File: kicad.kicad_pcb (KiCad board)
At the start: 2 copper layers, 68.6 x 53.3 mm, 8 parts, among them P1 Power, P2 Analog, P3 Digital, P4 Digital, P5 CONN_01X01, P6 CONN_01X01, P7 CONN_01X01, P8 CONN_01X01

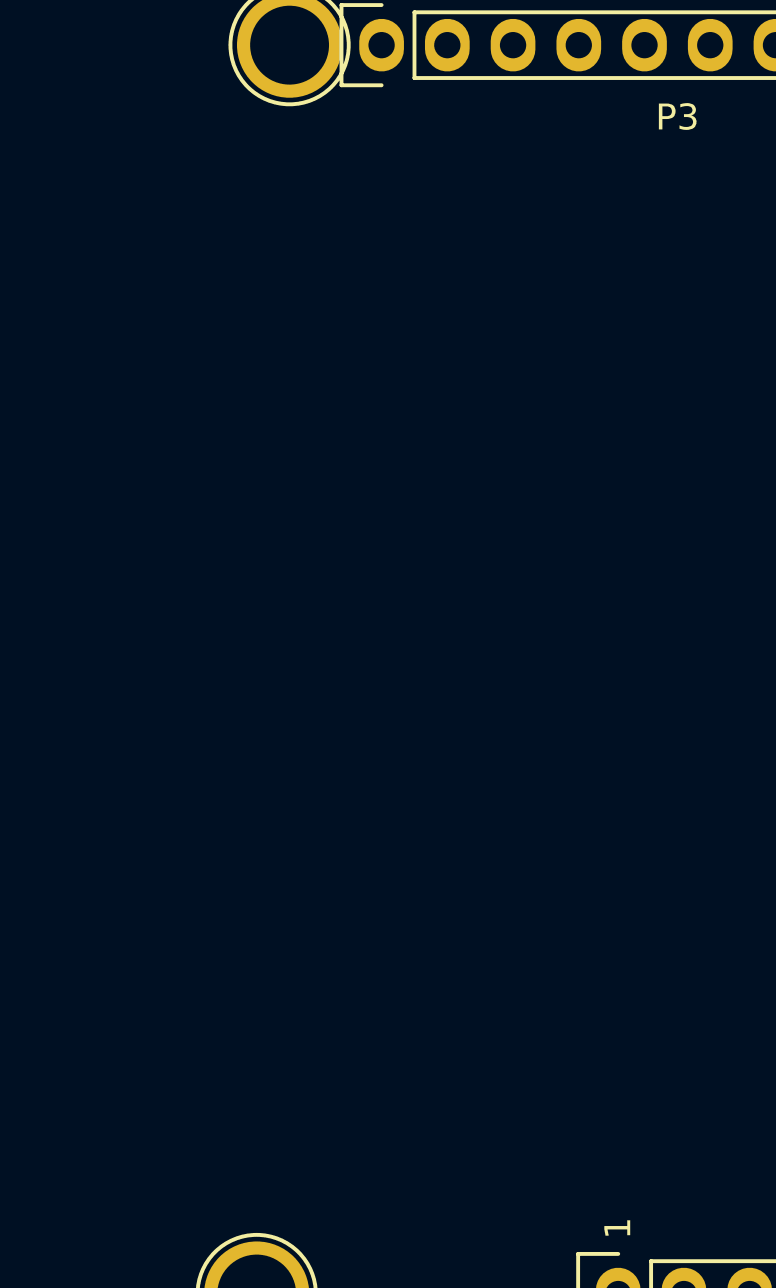
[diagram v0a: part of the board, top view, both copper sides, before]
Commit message: Add ATmega328P-PU
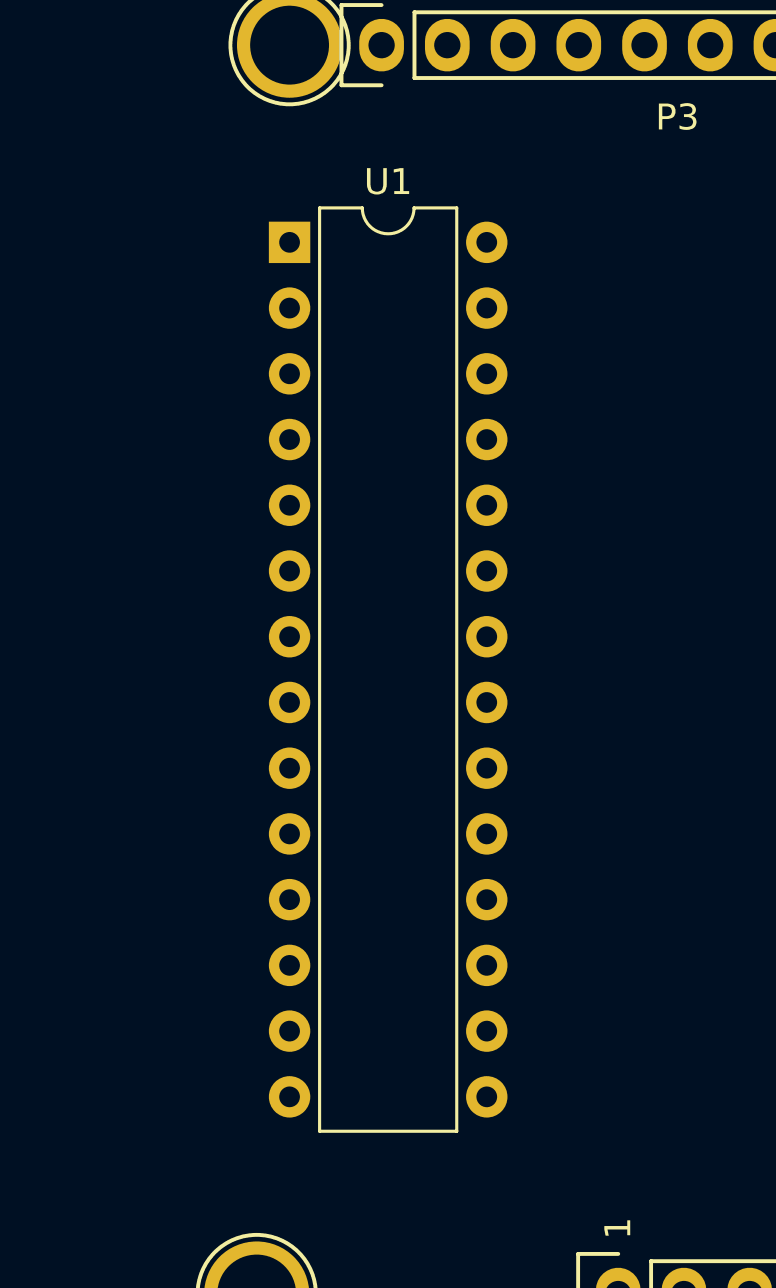
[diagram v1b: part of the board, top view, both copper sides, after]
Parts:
- added U1: ATmega328P-PU, Package_DIP:DIP-28_W7.62mm, F.Cu at (126.2, 83.2)
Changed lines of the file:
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@@
-(kicad_pcb (version 4) (host pcbnew 4.0.2-4+6225~38~ubuntu14.04.1-stable)
+(kicad_pcb (version 20171130) (host pcbnew 5.0.0+dfsg1-2)
   (general
-    (links 4)
-    (no_connects 4)
-    (area 104.572999 71.392 182.146334 127.594)
     (thickness 1.6)
     (drawings 27)
     (tracks 0)
     (zones 0)
-    (modules 8)
-    (nets 33)
+    (modules 9)
+    (nets 60)
   )
   (page A4)
@@
       (layerselection 0x00030_80000001)
       (usegerberextensions false)
+      (usegerberattributes false)
+      (usegerberadvancedattributes false)
+      (creategerberjobfile false)
       (excludeedgelayer true)
       (linewidth 0.100000)
@@
       (hpglpennumber 1)
       (hpglpenspeed 20)
-      (hpglpendiameter 15)
-      (hpglpenoverlay 2)
+      (hpglpendiameter 15.000000)
       (psnegative false)
       (psa4output false)
@@
   (net 31 "/12(MISO)")
   (net 32 "/11(**/MOSI)")
+  (net 33 "Net-(U1-Pad1)")
+  (net 34 "Net-(U1-Pad15)")
+  (net 35 "Net-(U1-Pad2)")
+  (net 36 "Net-(U1-Pad16)")
+  (net 37 "Net-(U1-Pad3)")
+  (net 38 "Net-(U1-Pad17)")
+  (net 39 "Net-(U1-Pad4)")
+  (net 40 "Net-(U1-Pad18)")
+  (net 41 "Net-(U1-Pad5)")
+  (net 42 "Net-(U1-Pad19)")
+  (net 43 "Net-(U1-Pad6)")
+  (net 44 "Net-(U1-Pad20)")
+  (net 45 "Net-(U1-Pad7)")
+  (net 46 "Net-(U1-Pad21)")
+  (net 47 "Net-(U1-Pad22)")
+  (net 48 "Net-(U1-Pad9)")
+  (net 49 "Net-(U1-Pad23)")
+  (net 50 "Net-(U1-Pad10)")
+  (net 51 "Net-(U1-Pad24)")
+  (net 52 "Net-(U1-Pad11)")
+  (net 53 "Net-(U1-Pad25)")
+  (net 54 "Net-(U1-Pad12)")
+  (net 55 "Net-(U1-Pad26)")
+  (net 56 "Net-(U1-Pad13)")
+  (net 57 "Net-(U1-Pad27)")
+  (net 58 "Net-(U1-Pad14)")
+  (net 59 "Net-(U1-Pad28)")
   (net_class Default "This is the default net class."
     (clearance 0.2)
@@
     (add_net "Net-(P7-Pad1)")
     (add_net "Net-(P8-Pad1)")
+    (add_net "Net-(U1-Pad1)")
+    (add_net "Net-(U1-Pad10)")
+    (add_net "Net-(U1-Pad11)")
+    (add_net "Net-(U1-Pad12)")
+    (add_net "Net-(U1-Pad13)")
+    (add_net "Net-(U1-Pad14)")
+    (add_net "Net-(U1-Pad15)")
+    (add_net "Net-(U1-Pad16)")
+    (add_net "Net-(U1-Pad17)")
+    (add_net "Net-(U1-Pad18)")
+    (add_net "Net-(U1-Pad19)")
+    (add_net "Net-(U1-Pad2)")
+    (add_net "Net-(U1-Pad20)")
+    (add_net "Net-(U1-Pad21)")
+    (add_net "Net-(U1-Pad22)")
+    (add_net "Net-(U1-Pad23)")
+    (add_net "Net-(U1-Pad24)")
+    (add_net "Net-(U1-Pad25)")
+    (add_net "Net-(U1-Pad26)")
+    (add_net "Net-(U1-Pad27)")
+    (add_net "Net-(U1-Pad28)")
+    (add_net "Net-(U1-Pad3)")
+    (add_net "Net-(U1-Pad4)")
+    (add_net "Net-(U1-Pad5)")
+    (add_net "Net-(U1-Pad6)")
+    (add_net "Net-(U1-Pad7)")
+    (add_net "Net-(U1-Pad9)")
+  )
+  (module Package_DIP:DIP-28_W7.62mm (layer F.Cu)
+    (at 126.238 83.185)
+    (descr "28-lead though-hole mounted DIP package, row spacing 7.62 mm (300 mils)")
+    (tags "THT DIP DIL PDIP 2.54mm 7.62mm 300mil")
+    (fp_text reference U1 (at 3.81 -2.33) (layer F.SilkS)
+      (effects (font (size 1 1) (thickness 0.15)))
+    )
+    (fp_text value ATmega328P-PU (at 3.81 35.35) (layer F.Fab)
+      (effects (font (size 1 1) (thickness 0.15)))
+    )
+    (fp_arc (start 3.81 -1.33) (end 2.81 -1.33) (angle -180) (layer F.SilkS) (width 0.12))
+    (fp_line (start 1.635 -1.27) (end 6.985 -1.27) (layer F.Fab) (width 0.1))
+    (fp_line (start 6.985 -1.27) (end 6.985 34.29) (layer F.Fab) (width 0.1))
+    (fp_line (start 6.985 34.29) (end 0.635 34.29) (layer F.Fab) (width 0.1))
+    (fp_line (start 0.635 34.29) (end 0.635 -0.27) (layer F.Fab) (width 0.1))
+    (fp_line (start 0.635 -0.27) (end 1.635 -1.27) (layer F.Fab) (width 0.1))
+    (fp_line (start 2.81 -1.33) (end 1.16 -1.33) (layer F.SilkS) (width 0.12))
+    (fp_line (start 1.16 -1.33) (end 1.16 34.35) (layer F.SilkS) (width 0.12))
+    (fp_line (start 1.16 34.35) (end 6.46 34.35) (layer F.SilkS) (width 0.12))
+    (fp_line (start 6.46 34.35) (end 6.46 -1.33) (layer F.SilkS) (width 0.12))
+    (fp_line (start 6.46 -1.33) (end 4.81 -1.33) (layer F.SilkS) (width 0.12))
+    (fp_line (start -1.1 -1.55) (end -1.1 34.55) (layer F.CrtYd) (width 0.05))
+    (fp_line (start -1.1 34.55) (end 8.7 34.55) (layer F.CrtYd) (width 0.05))
+    (fp_line (start 8.7 34.55) (end 8.7 -1.55) (layer F.CrtYd) (width 0.05))
+    (fp_line (start 8.7 -1.55) (end -1.1 -1.55) (layer F.CrtYd) (width 0.05))
+    (fp_text user %R (at 3.81 16.51) (layer F.Fab)
+      (effects (font (size 1 1) (thickness 0.15)))
+    )
+    (pad 1 thru_hole rect (at 0 0) (size 1.6 1.6) (drill 0.8) (layers *.Cu *.Mask)
+      (net 33 "Net-(U1-Pad1)"))
+    (pad 15 thru_hole oval (at 7.62 33.02) (size 1.6 1.6) (drill 0.8) (layers *.Cu *.Mask)
+      (net 34 "Net-(U1-Pad15)"))
+    (pad 2 thru_hole oval (at 0 2.54) (size 1.6 1.6) (drill 0.8) (layers *.Cu *.Mask)
+      (net 35 "Net-(U1-Pad2)"))
+    (pad 16 thru_hole oval (at 7.62 30.48) (size 1.6 1.6) (drill 0.8) (layers *.Cu *.Mask)
+      (net 36 "Net-(U1-Pad16)"))
+    (pad 3 thru_hole oval (at 0 5.08) (size 1.6 1.6) (drill 0.8) (layers *.Cu *.Mask)
+      (net 37 "Net-(U1-Pad3)"))
+    (pad 17 thru_hole oval (at 7.62 27.94) (size 1.6 1.6) (drill 0.8) (layers *.Cu *.Mask)
+      (net 38 "Net-(U1-Pad17)"))
+    (pad 4 thru_hole oval (at 0 7.62) (size 1.6 1.6) (drill 0.8) (layers *.Cu *.Mask)
+      (net 39 "Net-(U1-Pad4)"))
+    (pad 18 thru_hole oval (at 7.62 25.4) (size 1.6 1.6) (drill 0.8) (layers *.Cu *.Mask)
+      (net 40 "Net-(U1-Pad18)"))
+    (pad 5 thru_hole oval (at 0 10.16) (size 1.6 1.6) (drill 0.8) (layers *.Cu *.Mask)
+      (net 41 "Net-(U1-Pad5)"))
+    (pad 19 thru_hole oval (at 7.62 22.86) (size 1.6 1.6) (drill 0.8) (layers *.Cu *.Mask)
+      (net 42 "Net-(U1-Pad19)"))
+    (pad 6 thru_hole oval (at 0 12.7) (size 1.6 1.6) (drill 0.8) (layers *.Cu *.Mask)
+      (net 43 "Net-(U1-Pad6)"))
+    (pad 20 thru_hole oval (at 7.62 20.32) (size 1.6 1.6) (drill 0.8) (layers *.Cu *.Mask)
+      (net 44 "Net-(U1-Pad20)"))
+    (pad 7 thru_hole oval (at 0 15.24) (size 1.6 1.6) (drill 0.8) (layers *.Cu *.Mask)
+      (net 45 "Net-(U1-Pad7)"))
+    (pad 21 thru_hole oval (at 7.62 17.78) (size 1.6 1.6) (drill 0.8) (layers *.Cu *.Mask)
+      (net 46 "Net-(U1-Pad21)"))
+    (pad 8 thru_hole oval (at 0 17.78) (size 1.6 1.6) (drill 0.8) (layers *.Cu *.Mask)
+      (net 47 "Net-(U1-Pad22)"))
+    (pad 22 thru_hole oval (at 7.62 15.24) (size 1.6 1.6) (drill 0.8) (layers *.Cu *.Mask)
+      (net 47 "Net-(U1-Pad22)"))
+    (pad 9 thru_hole oval (at 0 20.32) (size 1.6 1.6) (drill 0.8) (layers *.Cu *.Mask)
+      (net 48 "Net-(U1-Pad9)"))
+    (pad 23 thru_hole oval (at 7.62 12.7) (size 1.6 1.6) (drill 0.8) (layers *.Cu *.Mask)
+      (net 49 "Net-(U1-Pad23)"))
+    (pad 10 thru_hole oval (at 0 22.86) (size 1.6 1.6) (drill 0.8) (layers *.Cu *.Mask)
+      (net 50 "Net-(U1-Pad10)"))
+    (pad 24 thru_hole oval (at 7.62 10.16) (size 1.6 1.6) (drill 0.8) (layers *.Cu *.Mask)
+      (net 51 "Net-(U1-Pad24)"))
+    (pad 11 thru_hole oval (at 0 25.4) (size 1.6 1.6) (drill 0.8) (layers *.Cu *.Mask)
+      (net 52 "Net-(U1-Pad11)"))
+    (pad 25 thru_hole oval (at 7.62 7.62) (size 1.6 1.6) (drill 0.8) (layers *.Cu *.Mask)
+      (net 53 "Net-(U1-Pad25)"))
+    (pad 12 thru_hole oval (at 0 27.94) (size 1.6 1.6) (drill 0.8) (layers *.Cu *.Mask)
+      (net 54 "Net-(U1-Pad12)"))
+    (pad 26 thru_hole oval (at 7.62 5.08) (size 1.6 1.6) (drill 0.8) (layers *.Cu *.Mask)
+      (net 55 "Net-(U1-Pad26)"))
+    (pad 13 thru_hole oval (at 0 30.48) (size 1.6 1.6) (drill 0.8) (layers *.Cu *.Mask)
+      (net 56 "Net-(U1-Pad13)"))
+    (pad 27 thru_hole oval (at 7.62 2.54) (size 1.6 1.6) (drill 0.8) (layers *.Cu *.Mask)
+      (net 57 "Net-(U1-Pad27)"))
+    (pad 14 thru_hole oval (at 0 33.02) (size 1.6 1.6) (drill 0.8) (layers *.Cu *.Mask)
+      (net 58 "Net-(U1-Pad14)"))
+    (pad 28 thru_hole oval (at 7.62 0) (size 1.6 1.6) (drill 0.8) (layers *.Cu *.Mask)
+      (net 59 "Net-(U1-Pad28)"))
+    (model ${KISYS3DMOD}/Package_DIP.3dshapes/DIP-28_W7.62mm.wrl
+      (at (xyz 0 0 0))
+      (scale (xyz 1 1 1))
+      (rotate (xyz 0 0 0))
+    )
   )
   (module Socket_Arduino_Uno:Socket_Strip_Arduino_1x08 locked (layer F.Cu)
@@
       (net 5 /Vin))
     (model ${KIPRJMOD}/Socket_Arduino_Uno.3dshapes/Socket_header_Arduino_1x08.wrl
-      (at (xyz 0.35 0 0))
+      (offset (xyz 8.889999866485596 0 0))
       (scale (xyz 1 1 1))
       (rotate (xyz 0 0 180))
@@
       (net 12 "/A5(SCL)"))
     (model ${KIPRJMOD}/Socket_Arduino_Uno.3dshapes/Socket_header_Arduino_1x06.wrl
-      (at (xyz 0.25 0 0))
+      (offset (xyz 6.349999904632568 0 0))
       (scale (xyz 1 1 1))
       (rotate (xyz 0 0 180))
@@
       (net 14 /8))
     (model ${KIPRJMOD}/Socket_Arduino_Uno.3dshapes/Socket_header_Arduino_1x10.wrl
-      (at (xyz 0.45 0 0))
+      (offset (xyz 11.42999982833862 0 0))
       (scale (xyz 1 1 1))
       (rotate (xyz 0 0 180))
@@
       (net 22 "/0(Rx)"))
     (model ${KIPRJMOD}/Socket_Arduino_Uno.3dshapes/Socket_header_Arduino_1x08.wrl
-      (at (xyz 0.35 0 0))
+      (offset (xyz 8.889999866485596 0 0))
       (scale (xyz 1 1 1))
       (rotate (xyz 0 0 180))
